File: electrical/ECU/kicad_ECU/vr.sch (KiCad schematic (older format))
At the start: 2 parts

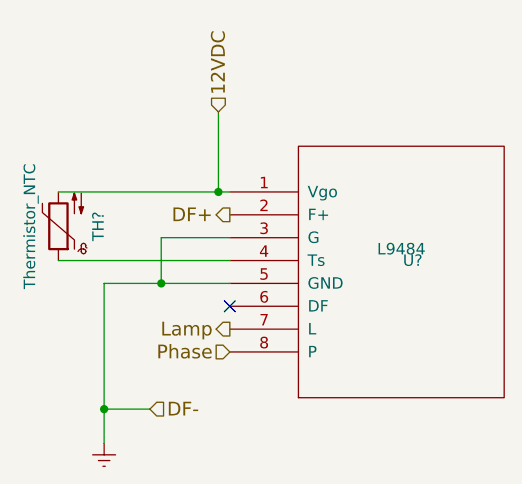
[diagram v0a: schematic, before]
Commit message: fixed some naming errors and initial round of double checking
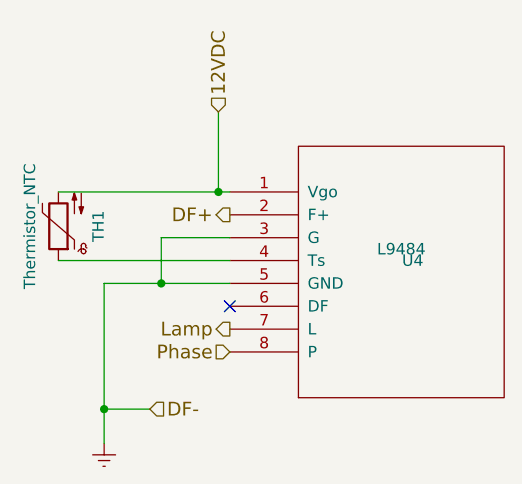
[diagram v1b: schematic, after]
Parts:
- gave numbers to parts that had none: 2
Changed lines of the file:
@@
 $EndDescr
 $Comp
-L L9484 U?
+L L9484 U4
 U 1 1 58AD6AAA
 P 6800 3700
-F 0 "U?" H 6850 3750 50  0000 C CNN
+F 0 "U4" H 6850 3750 50  0000 C CNN
 F 1 "L9484" H 6800 3800 50  0000 C CNN
 F 2 "MODULE" H 6800 3700 50  0001 C CNN
@@
 $EndComp
 $Comp
-L Thermistor_NTC TH?
+L Thermistor_NTC TH1
 U 1 1 58AD6AB1
 P 5300 3500
-F 0 "TH?" V 5125 3500 50  0000 C CNN
+F 0 "TH1" V 5125 3500 50  0000 C CNN
 F 1 "Thermistor_NTC" V 5425 3500 50  0000 C CNN
 F 2 "" H 5300 3550 50  0001 C CNN
@@
 Connection ~ 5750 3750
 $Comp
-L Earth #PWR?
+L Earth #PWR12
 U 1 1 58AD6ACC
 P 5500 4450
-F 0 "#PWR?" H 5500 4200 50  0001 C CNN
+F 0 "#PWR12" H 5500 4200 50  0001 C CNN
 F 1 "Earth" H 5500 4300 50  0001 C CNN
 F 2 "" H 5500 4450 50  0000 C CNN
